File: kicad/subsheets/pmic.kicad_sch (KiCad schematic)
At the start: 54 parts, among them U2 RK809-5

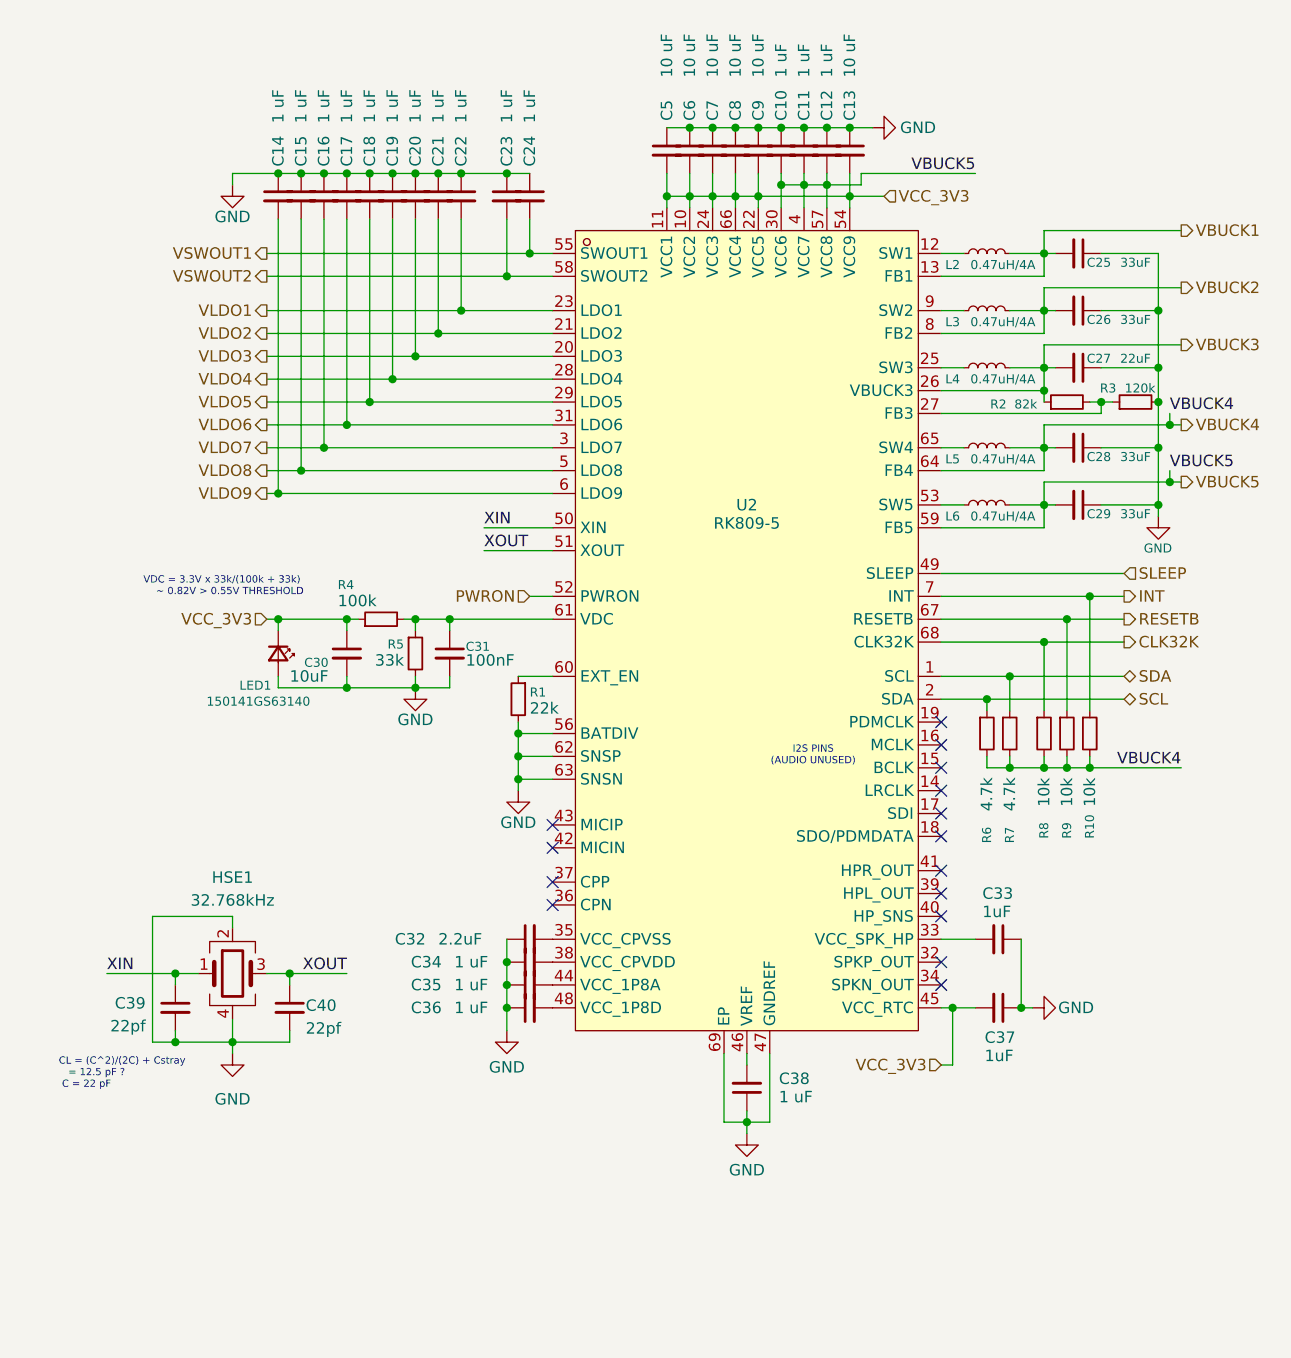
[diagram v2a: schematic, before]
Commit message: Add ports for FC and RK3566
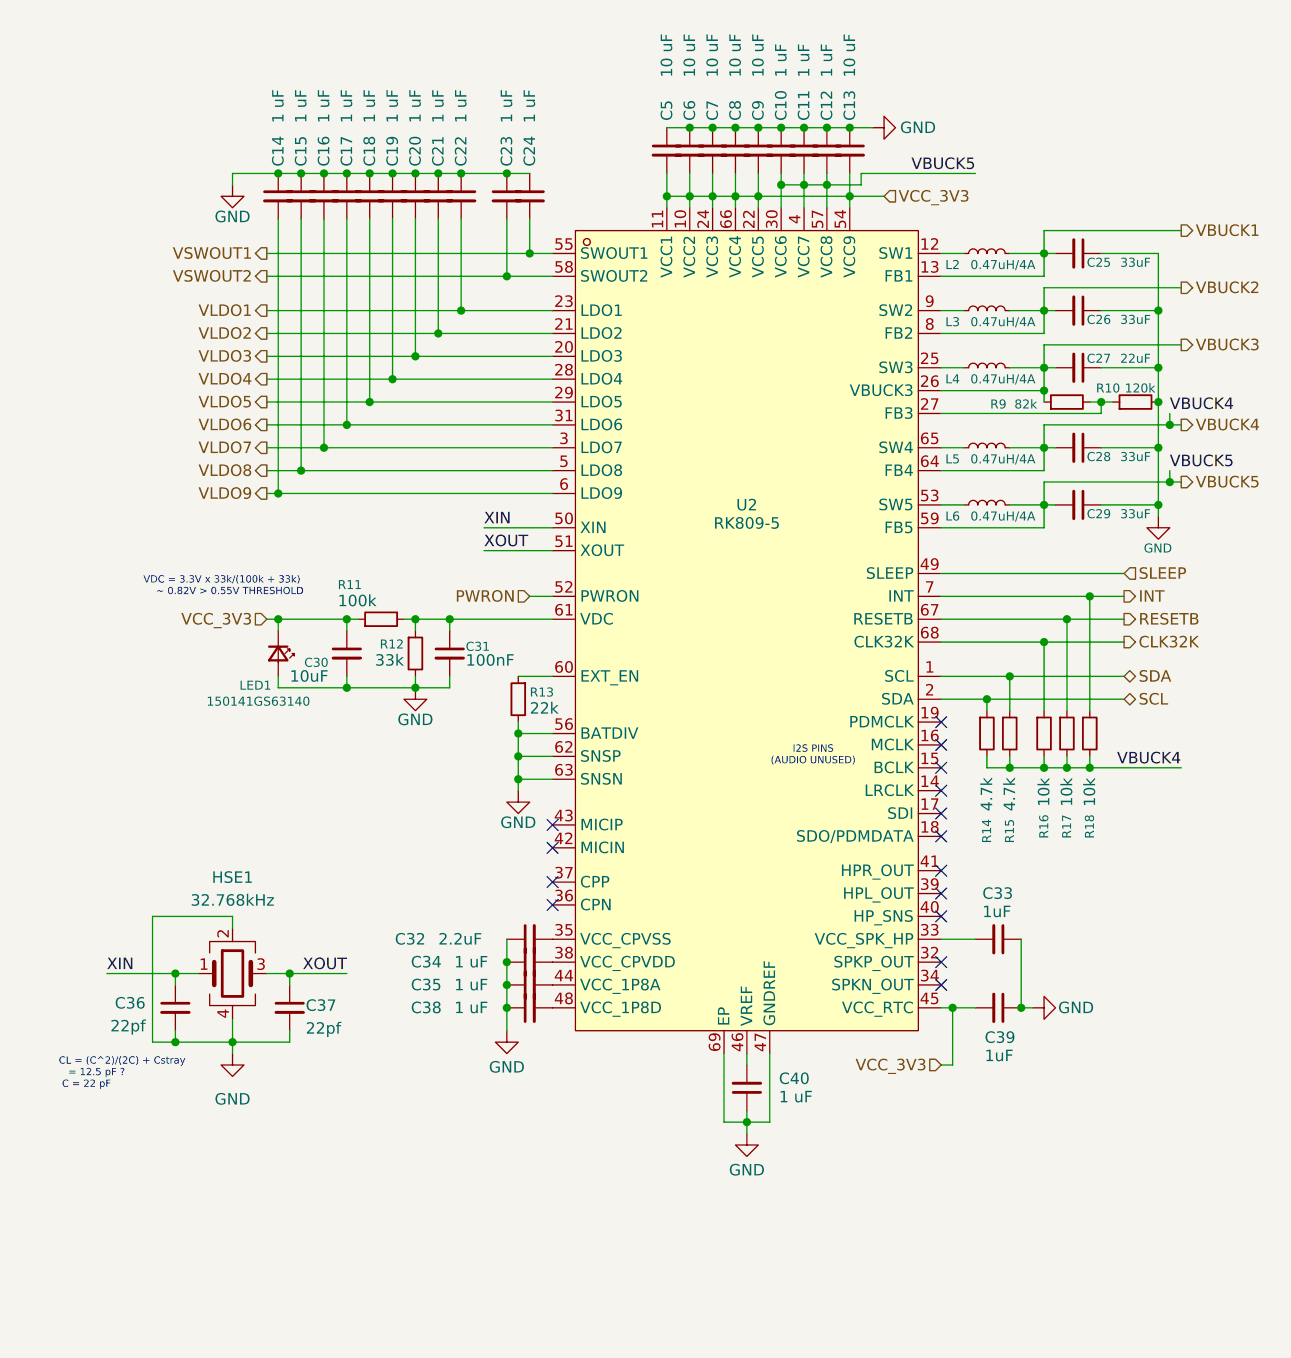
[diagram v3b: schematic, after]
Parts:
- renumbered C39 to C36, C40 to C37, C36 to C38, C37 to C39, C38 to C40, R3 to R10, R4 to R11, R5 to R12, R1 to R13, R6 to R14, R7 to R15, R8 to R16, R9 to R17, R10 to R18, R2 to R9
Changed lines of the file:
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@@
 		)
 	)
-	(label "XOUT"
-		(at 63.5 73.66 0)
+	(label "XIN"
+		(at 63.5 71.12 0)
 		(effects
 			(font
@@
 		)
 	)
-	(label "XIN"
-		(at 63.5 71.12 0)
+	(label "XOUT"
+		(at 63.5 73.66 0)
 		(effects
 			(font
@@
 		(on_board yes)
 		(dnp no)
-		(property "Reference" "#PWR07"
+		(property "Reference" "#PWR011"
 			(at 138.43 76.2 0)
 			(effects
@@
 			(project "srad-camera"
 				(path "/da62c771-e8c9-451f-8df1-ec995aadcb11/6bb226bc-8621-46e9-a0f1-5501f65ad069"
-					(reference "#PWR07")
+					(reference "#PWR011")
 					(unit 1)
 				)
@@
 		(on_board yes)
 		(dnp no)
-		(property "Reference" "R7"
+		(property "Reference" "R15"
 			(at 121.92 106.172 90)
 			(effects
@@
 			(project "srad-camera"
 				(path "/da62c771-e8c9-451f-8df1-ec995aadcb11/6bb226bc-8621-46e9-a0f1-5501f65ad069"
-					(reference "R7")
+					(reference "R15")
 					(unit 1)
 				)
@@
 		(on_board yes)
 		(dnp no)
-		(property "Reference" "C38"
+		(property "Reference" "C40"
 			(at 96.266 132.334 0)
 			(effects
@@
 			(project "srad-camera"
 				(path "/da62c771-e8c9-451f-8df1-ec995aadcb11/6bb226bc-8621-46e9-a0f1-5501f65ad069"
-					(reference "C38")
+					(reference "C40")
 					(unit 1)
 				)
@@
 		(on_board yes)
 		(dnp no)
-		(property "Reference" "R6"
+		(property "Reference" "R14"
 			(at 119.38 106.172 90)
 			(effects
@@
 			(project "srad-camera"
 				(path "/da62c771-e8c9-451f-8df1-ec995aadcb11/6bb226bc-8621-46e9-a0f1-5501f65ad069"
-					(reference "R6")
+					(reference "R14")
 					(unit 1)
 				)
@@
 		(on_board yes)
 		(dnp no)
-		(property "Reference" "#PWR013"
+		(property "Reference" "#PWR017"
 			(at 92.71 144.78 0)
 			(effects
@@
 			(project "srad-camera"
 				(path "/da62c771-e8c9-451f-8df1-ec995aadcb11/6bb226bc-8621-46e9-a0f1-5501f65ad069"
-					(reference "#PWR013")
+					(reference "#PWR017")
 					(unit 1)
 				)
@@
 		(on_board yes)
 		(dnp no)
-		(property "Reference" "C36"
+		(property "Reference" "C38"
 			(at 55.372 124.46 90)
 			(effects
@@
 			(project "srad-camera"
 				(path "/da62c771-e8c9-451f-8df1-ec995aadcb11/6bb226bc-8621-46e9-a0f1-5501f65ad069"
-					(reference "C36")
+					(reference "C38")
 					(unit 1)
 				)
@@
 		(on_board yes)
 		(dnp no)
-		(property "Reference" "#PWR08"
+		(property "Reference" "#PWR012"
 			(at 55.88 95.25 0)
 			(effects
@@
 			(project "srad-camera"
 				(path "/da62c771-e8c9-451f-8df1-ec995aadcb11/6bb226bc-8621-46e9-a0f1-5501f65ad069"
-					(reference "#PWR08")
+					(reference "#PWR012")
 					(unit 1)
 				)
@@
 		(on_board yes)
 		(dnp no)
-		(property "Reference" "R5"
+		(property "Reference" "R12"
 			(at 54.61 84.074 0)
 			(effects
@@
 			(project "srad-camera"
 				(path "/da62c771-e8c9-451f-8df1-ec995aadcb11/6bb226bc-8621-46e9-a0f1-5501f65ad069"
-					(reference "R5")
+					(reference "R12")
 					(unit 1)
 				)
@@
 		(on_board yes)
 		(dnp no)
-		(property "Reference" "#PWR06"
+		(property "Reference" "#PWR010"
 			(at 35.56 39.37 0)
 			(effects
@@
 			(project "srad-camera"
 				(path "/da62c771-e8c9-451f-8df1-ec995aadcb11/6bb226bc-8621-46e9-a0f1-5501f65ad069"
-					(reference "#PWR06")
+					(reference "#PWR010")
 					(unit 1)
 				)
@@
 		(on_board yes)
 		(dnp no)
-		(property "Reference" "R10"
+		(property "Reference" "R18"
 			(at 130.81 105.664 90)
 			(effects
@@
 			(project "srad-camera"
 				(path "/da62c771-e8c9-451f-8df1-ec995aadcb11/6bb226bc-8621-46e9-a0f1-5501f65ad069"
-					(reference "R10")
+					(reference "R18")
 					(unit 1)
 				)
@@
 		(on_board yes)
 		(dnp no)
-		(property "Reference" "R1"
+		(property "Reference" "R13"
 			(at 68.58 89.408 0)
 			(effects
@@
 			(project "srad-camera"
 				(path "/da62c771-e8c9-451f-8df1-ec995aadcb11/6bb226bc-8621-46e9-a0f1-5501f65ad069"
-					(reference "R1")
+					(reference "R13")
 					(unit 1)
 				)
@@
 		(on_board yes)
 		(dnp no)
-		(property "Reference" "C40"
+		(property "Reference" "C37"
 			(at 43.688 124.206 0)
 			(effects
@@
 			(project "srad-camera"
 				(path "/da62c771-e8c9-451f-8df1-ec995aadcb11/6bb226bc-8621-46e9-a0f1-5501f65ad069"
-					(reference "C40")
+					(reference "C37")
 					(unit 1)
 				)
@@
 		(on_board yes)
 		(dnp no)
-		(property "Reference" "R2"
+		(property "Reference" "R9"
 			(at 120.65 57.404 90)
 			(effects
@@
 			(project "srad-camera"
 				(path "/da62c771-e8c9-451f-8df1-ec995aadcb11/6bb226bc-8621-46e9-a0f1-5501f65ad069"
-					(reference "R2")
+					(reference "R9")
 					(unit 1)
 				)
@@
 		(on_board yes)
 		(dnp no)
-		(property "Reference" "R4"
+		(property "Reference" "R11"
 			(at 47.244 77.47 90)
 			(effects
@@
 			(project "srad-camera"
 				(path "/da62c771-e8c9-451f-8df1-ec995aadcb11/6bb226bc-8621-46e9-a0f1-5501f65ad069"
-					(reference "R4")
+					(reference "R11")
 					(unit 1)
 				)
@@
 		(dnp no)
 		(fields_autoplaced yes)
-		(property "Reference" "#PWR014"
+		(property "Reference" "#PWR016"
 			(at 35.56 135.89 0)
 			(effects
@@
 			(project "srad-camera"
 				(path "/da62c771-e8c9-451f-8df1-ec995aadcb11/6bb226bc-8621-46e9-a0f1-5501f65ad069"
-					(reference "#PWR014")
+					(reference "#PWR016")
 					(unit 1)
 				)
@@
 		(on_board yes)
 		(dnp no)
-		(property "Reference" "C37"
+		(property "Reference" "C39"
 			(at 119.126 127.762 90)
 			(effects
@@
 			(project "srad-camera"
 				(path "/da62c771-e8c9-451f-8df1-ec995aadcb11/6bb226bc-8621-46e9-a0f1-5501f65ad069"
-					(reference "C37")
+					(reference "C39")
 					(unit 1)
 				)
@@
 		(on_board yes)
 		(dnp no)
-		(property "Reference" "C39"
+		(property "Reference" "C36"
 			(at 25.908 123.952 0)
 			(effects
@@
 			(project "srad-camera"
 				(path "/da62c771-e8c9-451f-8df1-ec995aadcb11/6bb226bc-8621-46e9-a0f1-5501f65ad069"
-					(reference "C39")
+					(reference "C36")
 					(unit 1)
 				)
@@
 		(on_board yes)
 		(dnp no)
-		(property "Reference" "#PWR012"
+		(property "Reference" "#PWR015"
 			(at 66.04 133.35 0)
 			(effects
@@
 			(project "srad-camera"
 				(path "/da62c771-e8c9-451f-8df1-ec995aadcb11/6bb226bc-8621-46e9-a0f1-5501f65ad069"
-					(reference "#PWR012")
+					(reference "#PWR015")
 					(unit 1)
 				)
@@
 		(on_board yes)
 		(dnp no)
-		(property "Reference" "#PWR09"
+		(property "Reference" "#PWR013"
 			(at 67.31 106.68 0)
 			(effects
@@
 			(project "srad-camera"
 				(path "/da62c771-e8c9-451f-8df1-ec995aadcb11/6bb226bc-8621-46e9-a0f1-5501f65ad069"
-					(reference "#PWR09")
+					(reference "#PWR013")
 					(unit 1)
 				)
@@
 		(on_board yes)
 		(dnp no)
-		(property "Reference" "#PWR011"
+		(property "Reference" "#PWR014"
 			(at 130.81 124.46 0)
 			(effects
@@
 			(project "srad-camera"
 				(path "/da62c771-e8c9-451f-8df1-ec995aadcb11/6bb226bc-8621-46e9-a0f1-5501f65ad069"
-					(reference "#PWR011")
+					(reference "#PWR014")
 					(unit 1)
 				)
@@
 		(on_board yes)
 		(dnp no)
-		(property "Reference" "R8"
+		(property "Reference" "R16"
 			(at 125.73 105.664 90)
 			(effects
@@
 			(project "srad-camera"
 				(path "/da62c771-e8c9-451f-8df1-ec995aadcb11/6bb226bc-8621-46e9-a0f1-5501f65ad069"
-					(reference "R8")
+					(reference "R16")
 					(unit 1)
 				)
@@
 		(on_board yes)
 		(dnp no)
-		(property "Reference" "R3"
+		(property "Reference" "R10"
 			(at 132.842 55.626 90)
 			(effects
@@
 			(project "srad-camera"
 				(path "/da62c771-e8c9-451f-8df1-ec995aadcb11/6bb226bc-8621-46e9-a0f1-5501f65ad069"
-					(reference "R3")
+					(reference "R10")
 					(unit 1)
 				)
@@
 		(on_board yes)
 		(dnp no)
-		(property "Reference" "R9"
+		(property "Reference" "R17"
 			(at 128.27 105.664 90)
 			(effects
@@
 			(project "srad-camera"
 				(path "/da62c771-e8c9-451f-8df1-ec995aadcb11/6bb226bc-8621-46e9-a0f1-5501f65ad069"
-					(reference "R9")
+					(reference "R17")
 					(unit 1)
 				)
@@
 		(on_board yes)
 		(dnp no)
-		(property "Reference" "#PWR04"
+		(property "Reference" "#PWR09"
 			(at 113.03 26.67 0)
 			(effects
@@
 			(project "srad-camera"
 				(path "/da62c771-e8c9-451f-8df1-ec995aadcb11/6bb226bc-8621-46e9-a0f1-5501f65ad069"
-					(reference "#PWR04")
+					(reference "#PWR09")
 					(unit 1)
 				)

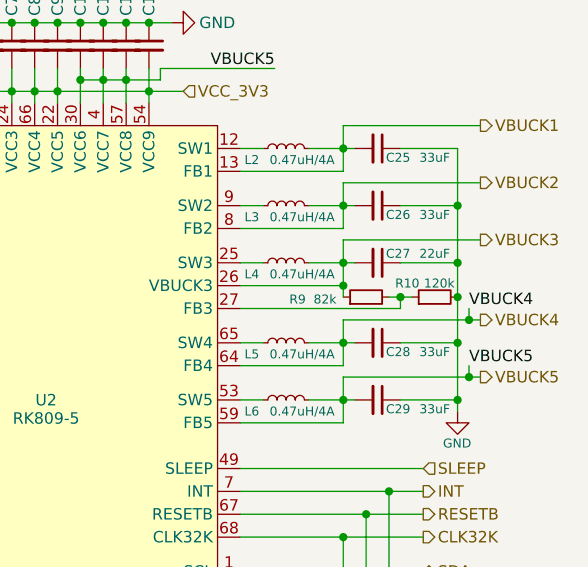
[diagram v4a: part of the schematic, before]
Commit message: Adjust root sheet
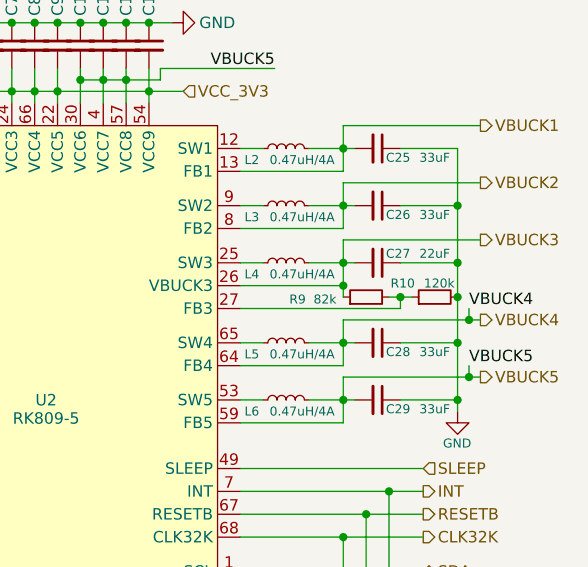
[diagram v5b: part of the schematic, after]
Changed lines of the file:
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@@
 		(dnp no)
 		(property "Reference" "R10"
-			(at 132.842 55.626 90)
+			(at 132.334 55.626 90)
 			(effects
 				(font
